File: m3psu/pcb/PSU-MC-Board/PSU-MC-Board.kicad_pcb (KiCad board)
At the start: 2 copper layers, 40 x 40 mm, 60 parts, among them IC1 STM32F405RxTx, IC2 TPS62152, IC3 MCP2562, IC4 LTC4353, IC5 LTC4151, J1 WEST TOP, J2 WEST BOT, J3 NORTH TOP, J4 EAST TOP, J5 EAST BOT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

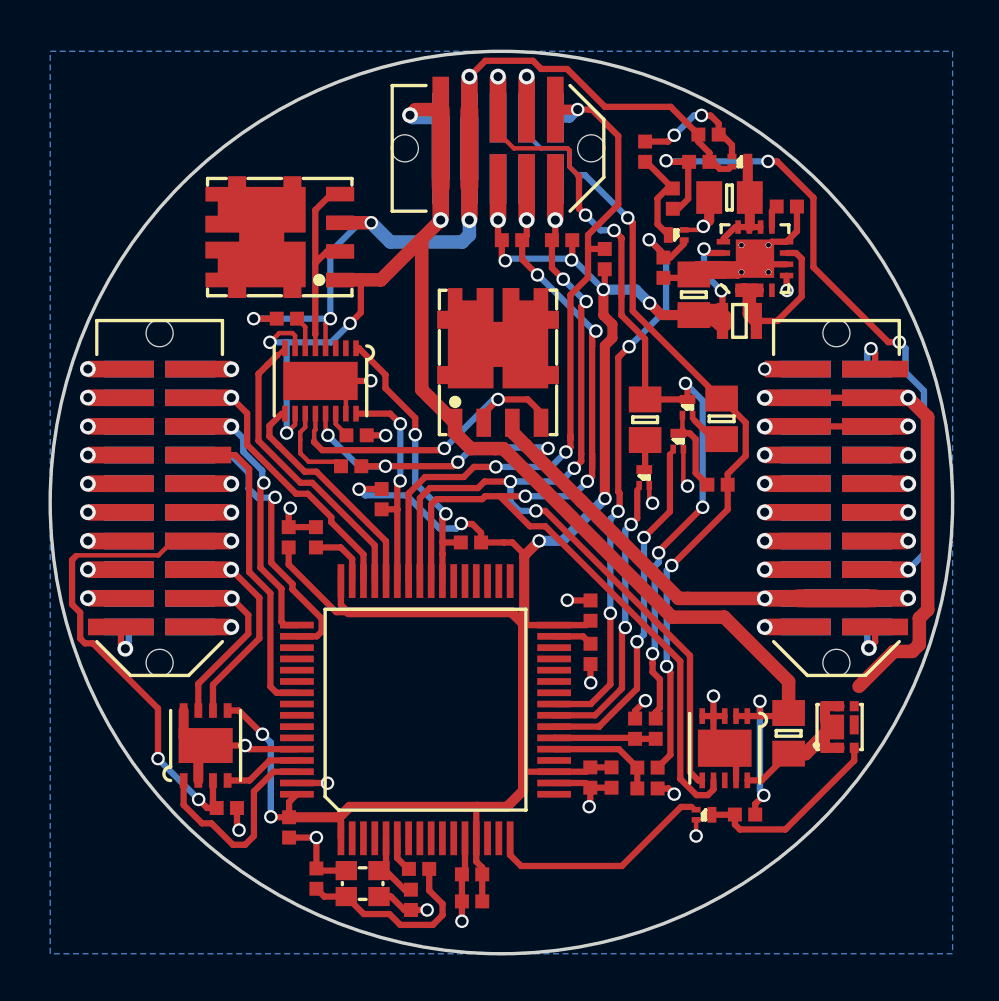
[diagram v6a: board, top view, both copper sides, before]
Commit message: Fixed the pin label problem (note that the problem isn't actually solved yet.)
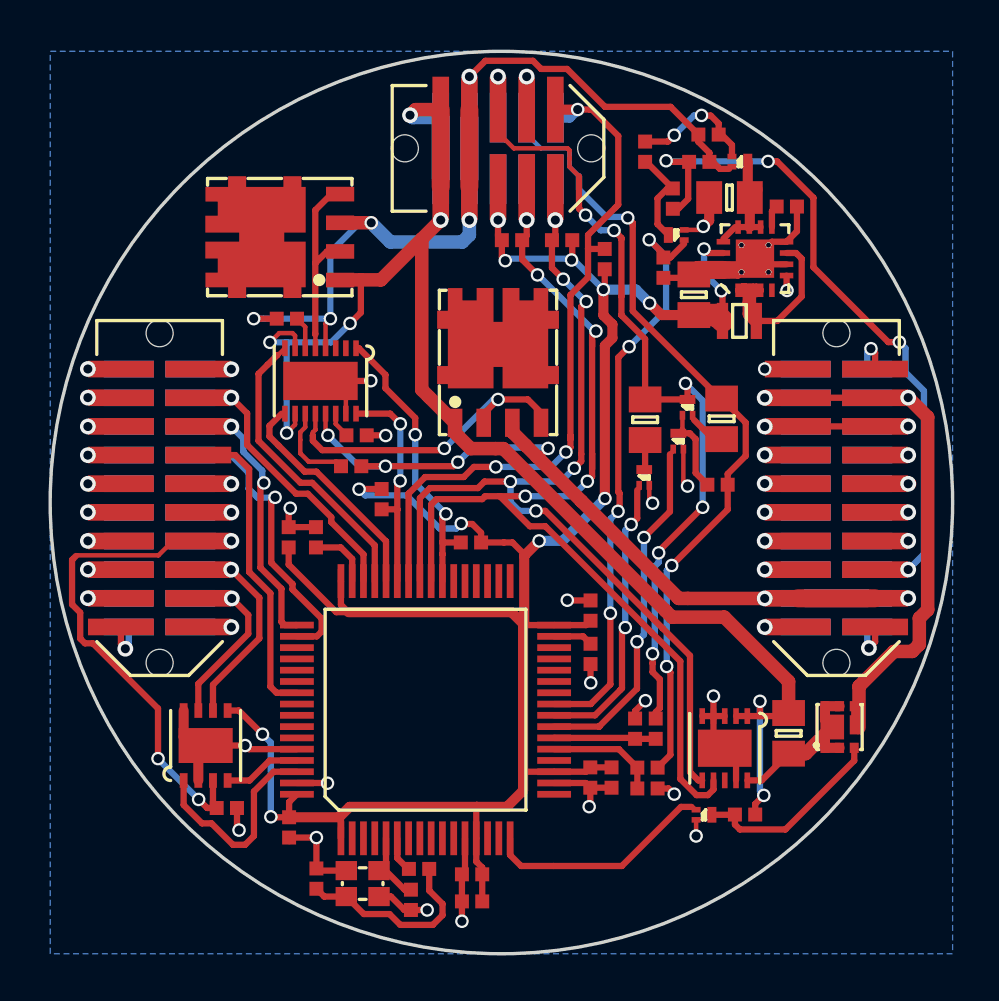
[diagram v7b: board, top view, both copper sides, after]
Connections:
- IC1 pad 10: Net-(IC1-Pad10) -> (no net)
- IC1 pad 11: Net-(IC1-Pad11) -> (no net)
- IC1 pad 14: Net-(IC1-Pad14) -> (no net)
- IC1 pad 15: Net-(IC1-Pad15) -> (no net)
- IC1 pad 17: Net-(IC1-Pad17) -> (no net)
- IC1 pad 2: Net-(IC1-Pad2) -> (no net)
- IC1 pad 20: Net-(IC1-Pad20) -> (no net)
- IC1 pad 26: Net-(IC1-Pad26) -> (no net)
- IC1 pad 27: Net-(IC1-Pad27) -> (no net)
- IC1 pad 28: Net-(IC1-Pad28) -> (no net)
- IC1 pad 29: Net-(IC1-Pad29) -> (no net)
- IC1 pad 3: Net-(IC1-Pad3) -> (no net)
- IC1 pad 30: Net-(IC1-Pad30) -> (no net)
- IC1 pad 33: Net-(IC1-Pad33) -> (no net)
- IC1 pad 34: Net-(IC1-Pad34) -> (no net)
- IC1 pad 35: Net-(IC1-Pad35) -> (no net)
- IC1 pad 36: Net-(IC1-Pad36) -> (no net)
- IC1 pad 37: Net-(IC1-Pad37) -> (no net)
- IC1 pad 38: Net-(IC1-Pad38) -> (no net)
- IC1 pad 4: Net-(IC1-Pad4) -> (no net)
- IC1 pad 51: Net-(IC1-Pad51) -> (no net)
- IC1 pad 52: Net-(IC1-Pad52) -> (no net)
- IC1 pad 53: Net-(IC1-Pad53) -> (no net)
- IC1 pad 54: Net-(IC1-Pad54) -> (no net)
- IC1 pad 56: Net-(IC1-Pad56) -> (no net)
- IC1 pad 57: Net-(IC1-Pad57) -> (no net)
- IC1 pad 58: Net-(IC1-Pad58) -> (no net)
- IC1 pad 59: Net-(IC1-Pad59) -> (no net)
- IC1 pad 7: Net-(IC1-Pad7) -> (no net)
- IC1 pad 8: Net-(IC1-Pad8) -> (no net)
- IC1 pad 9: Net-(IC1-Pad9) -> (no net)
- IC2 pad 4: Net-(IC2-Pad4) -> (no net)
- IC4 pad 2: Net-(IC4-Pad2) -> (no net)
- IC4 pad 3: Net-(IC4-Pad3) -> (no net)
- IC5 pad 8: Net-(IC5-Pad8) -> (no net)
- Q1 pad D: (no net) -> Net-(Q1-PadD)
- Q1 pad G: (no net) -> /~SHUTDOWN
- Q1 pad S: (no net) -> GND
- Q2 pad D: (no net) -> Net-(C12-Pad1)
- Q2 pad G: (no net) -> Net-(Q2-PadG)
- Q2 pad S: (no net) -> VBATT
- Q3 pad D: (no net) -> Net-(Q3-PadD)
- Q3 pad G: (no net) -> /BLEED_BATT2
- Q3 pad S: (no net) -> GND
- Q6 pad D: (no net) -> /BATT1
- Q6 pad G: (no net) -> Net-(Q3-PadD)
- Q6 pad S: (no net) -> Net-(Q6-PadS)
- Q7 pad D: (no net) -> Net-(Q7-PadD)
- Q7 pad G: (no net) -> /BLEED_BATT1
- Q7 pad S: (no net) -> GND
- Q8 pad D: (no net) -> /PYRO_SO
- Q8 pad G: (no net) -> Net-(Q8-PadG)
- Q8 pad S: (no net) -> Net-(IC5-Pad10)
- Q9 pad D: (no net) -> Net-(Q8-PadG)
- Q9 pad G: (no net) -> /EN_PYRO
- Q9 pad S: (no net) -> GND
- R12 pad 2: Net-(Q3-Pad3) -> Net-(Q3-PadD)
- R13 pad 2: Net-(Q6-Pad2) -> Net-(Q6-PadS)
- R14 pad 2: Net-(Q7-Pad3) -> Net-(Q7-PadD)
- R16 pad 2: Net-(Q8-Pad1) -> Net-(Q8-PadG)
- R4 pad 2: Net-(Q1-Pad3) -> Net-(Q1-PadD)
- R5 pad 2: Net-(Q2-Pad1) -> Net-(Q2-PadG)
- R6 pad 1: Net-(Q2-Pad1) -> Net-(Q2-PadG)
- R6 pad 2: Net-(Q1-Pad3) -> Net-(Q1-PadD)
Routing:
- net Net-(Q8-PadG): track 0.00 -> 8.68 mm
- net Net-(Q8-Pad1): track 8.68 -> 0.00 mm
- net Net-(Q2-PadG): track 0.00 -> 5.68 mm, vias 0 -> 2
- net Net-(Q2-Pad1): track 5.68 -> 0.00 mm, vias 2 -> 0
- net Net-(Q1-PadD): track 0.00 -> 4.48 mm
- net Net-(Q1-Pad3): track 4.48 -> 0.00 mm
- net Net-(Q3-PadD): track 0.00 -> 3.99 mm
- net Net-(Q3-Pad3): track 3.99 -> 0.00 mm
- net (no net): track 3.30 -> 0.00 mm, vias 3 -> 0
- net GND: track 78.9 -> 82.1 mm, vias 25 -> 28
- net /PYRO_SO: track 24.9 -> 27.6 mm
- net Net-(Q6-PadS): track 0.00 -> 1.81 mm
- net Net-(Q6-Pad2): track 1.81 -> 0.00 mm
- net Net-(Q7-PadD): track 0.00 -> 1.38 mm
- net Net-(Q7-Pad3): track 1.38 -> 0.00 mm

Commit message: Added in power switch line to MCU. Added silkscreen for some resistor areas in MC and Li-ion board.
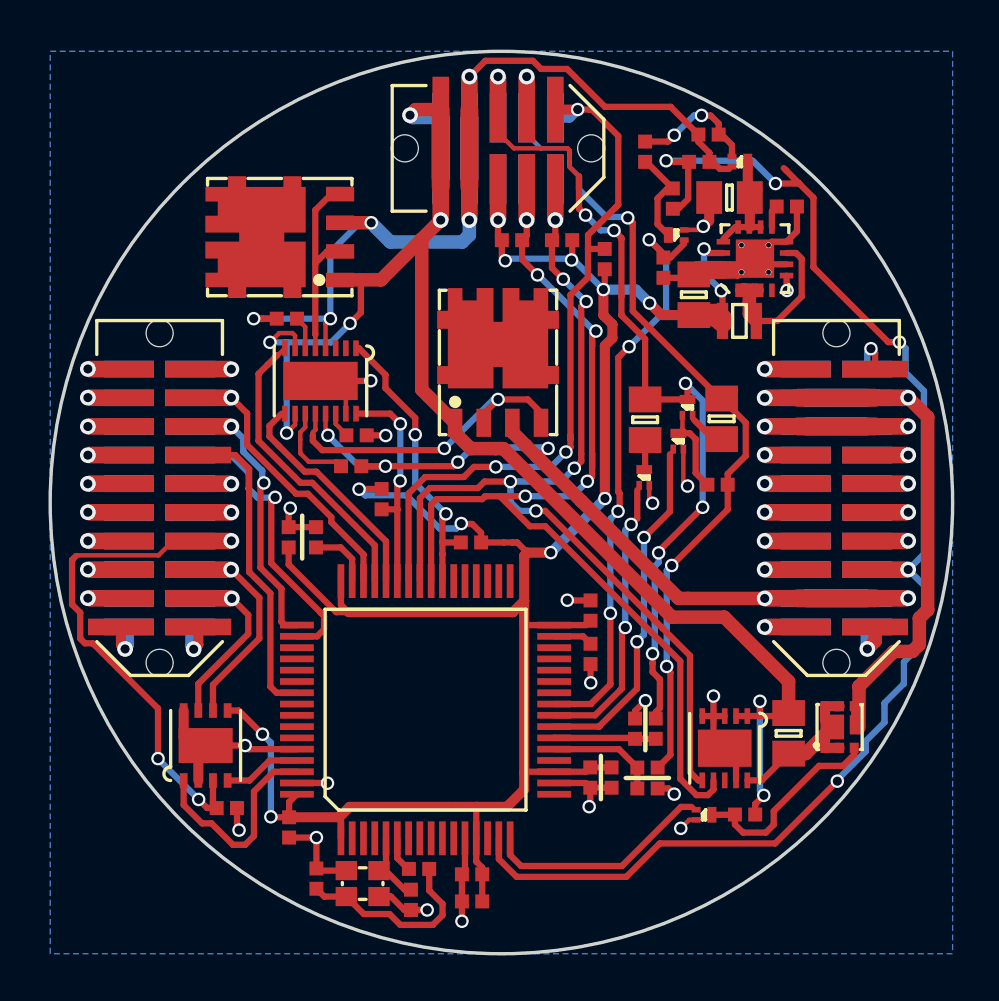
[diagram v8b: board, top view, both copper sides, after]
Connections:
- IC1 pad 15: (no net) -> /PWR
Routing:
- net /PWR: track 33.2 -> 63.6 mm, vias 4 -> 5
- net /PYRO_SO: track 27.6 -> 30.3 mm
- net /PYRO_SI: track 10.00 -> 12.7 mm
- net /PYRO2: track 4.81 -> 3.28 mm
- net GND: track 82.1 -> 81.2 mm
